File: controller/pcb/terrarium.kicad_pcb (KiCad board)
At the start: 2 copper layers, 90 x 90 mm, 55 parts, among them Q1 S8050, Q2 S8050, Q3 S8050, SW1 SW_Push, SW2 SW_Push, U1 ESP32-WROOM-32, U2 DS3231M, U3 LM1117-3.3

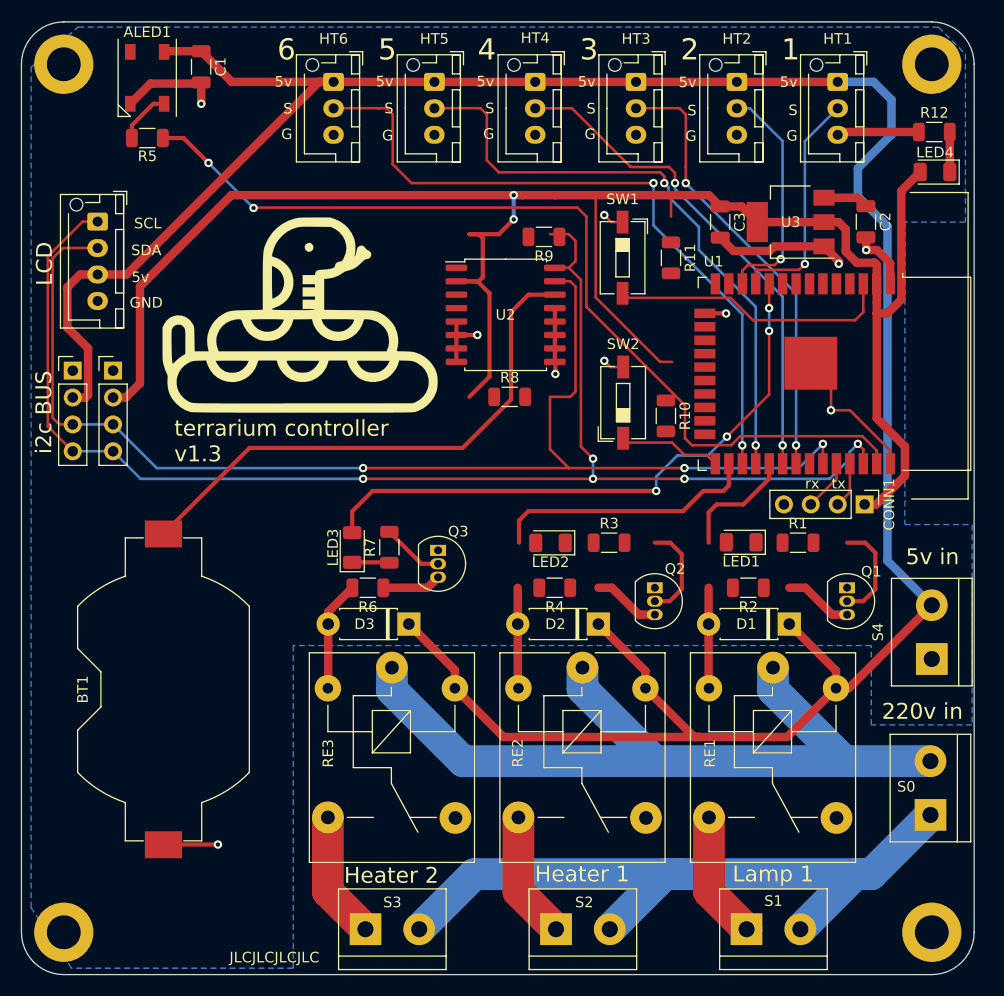
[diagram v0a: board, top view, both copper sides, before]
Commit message: pcb: developing smd layout
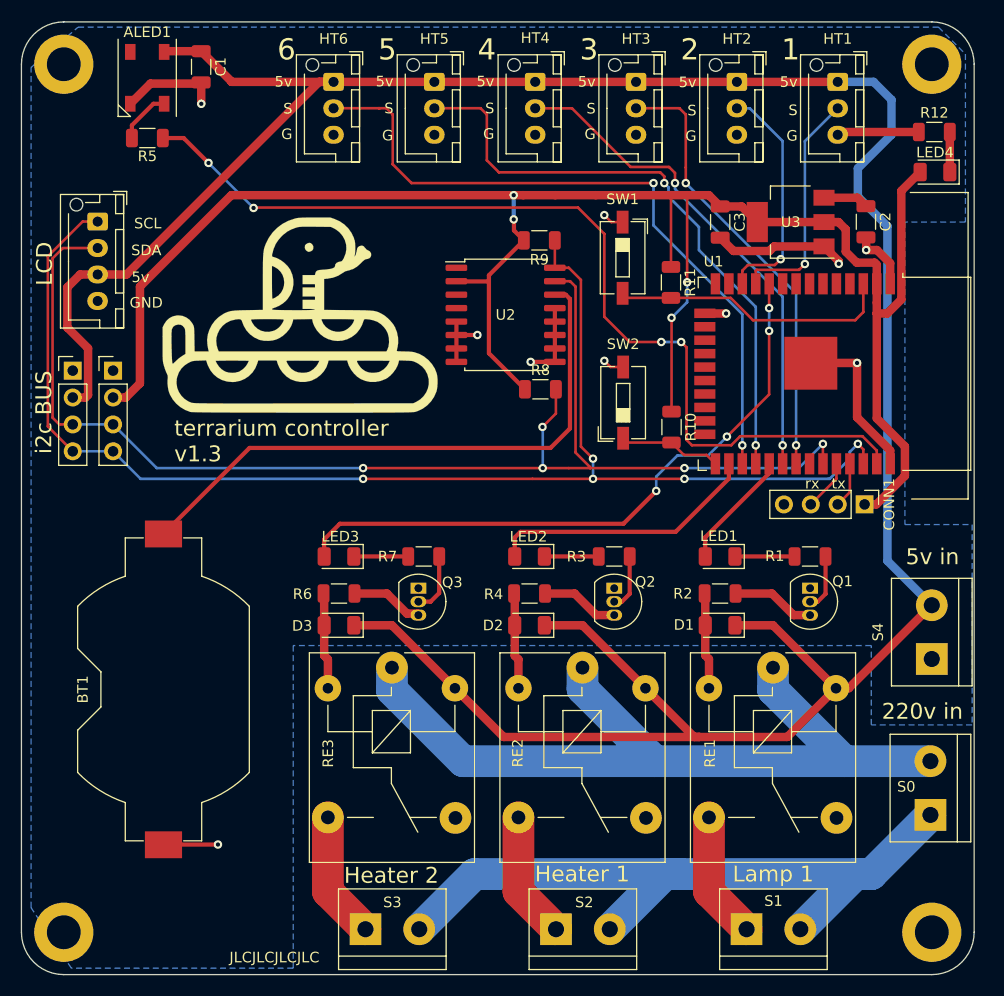
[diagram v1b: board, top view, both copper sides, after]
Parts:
- D1, D2, D3: footprint Diode_THT:D_DO-41_SOD81_P7.62mm_Horizontal -> Diode_SMD:D_1206_3216Metric
- moved D3 6.60 mm to (71.0, 80.0)
- moved D1 6.54 mm to (107.0, 80.0)
- moved D2 6.51 mm to (89.0, 80.0)
- moved Q3 4.03 mm to (78.5, 76.5)
- moved Q2 3.84 mm to (97.0, 76.5)
- moved Q1 3.50 mm to (115.5, 76.5)
- moved R7 3.36 mm to (79.0, 73.5), turned to 0 degrees
- moved R8 2.99 mm to (90.0, 57.7)
- moved R6 2.78 mm to (71.0, 77.0)
- moved R2 2.72 mm to (107.0, 77.0)
- moved R4 2.44 mm to (89.0, 77.0)
- moved LED1 2.40 mm to (107.0, 73.5)
- moved LED2 2.36 mm to (89.0, 73.5)
- moved R11 2.32 mm to (102.4, 47.6)
- moved R1 1.73 mm to (115.5, 73.5)
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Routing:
- net +5V: track 255.6 -> 268.0 mm
- net SDA: track 119.4 -> 125.1 mm, vias 3 -> 5
- net Net-(LED1-Pad1): track 0.00 -> 5.64 mm
- net GND: track 72.9 -> 78.3 mm
- net Net-(BT1-Pad1): track 51.2 -> 56.4 mm
- net Net-(LED2-Pad1): track 0.00 -> 5.14 mm
- net Net-(Q1-Pad2): track 9.63 -> 5.30 mm
- net Net-(Q2-Pad2): track 9.30 -> 5.30 mm
- net G25: track 57.2 -> 60.6 mm
- net SCL: track 132.2 -> 129.3 mm
- net G23: track 88.4 -> 91.3 mm, vias 2 -> 4
- net +3V3: track 181.9 -> 183.9 mm, vias 2 -> 4
- net Net-(LED3-Pad1): track 3.53 -> 5.14 mm
- net Net-(Q1-Pad3): track 6.51 -> 7.88 mm
- net Net-(Q3-Pad3): track 5.58 -> 6.93 mm
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
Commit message: Add copper plate, minor changes
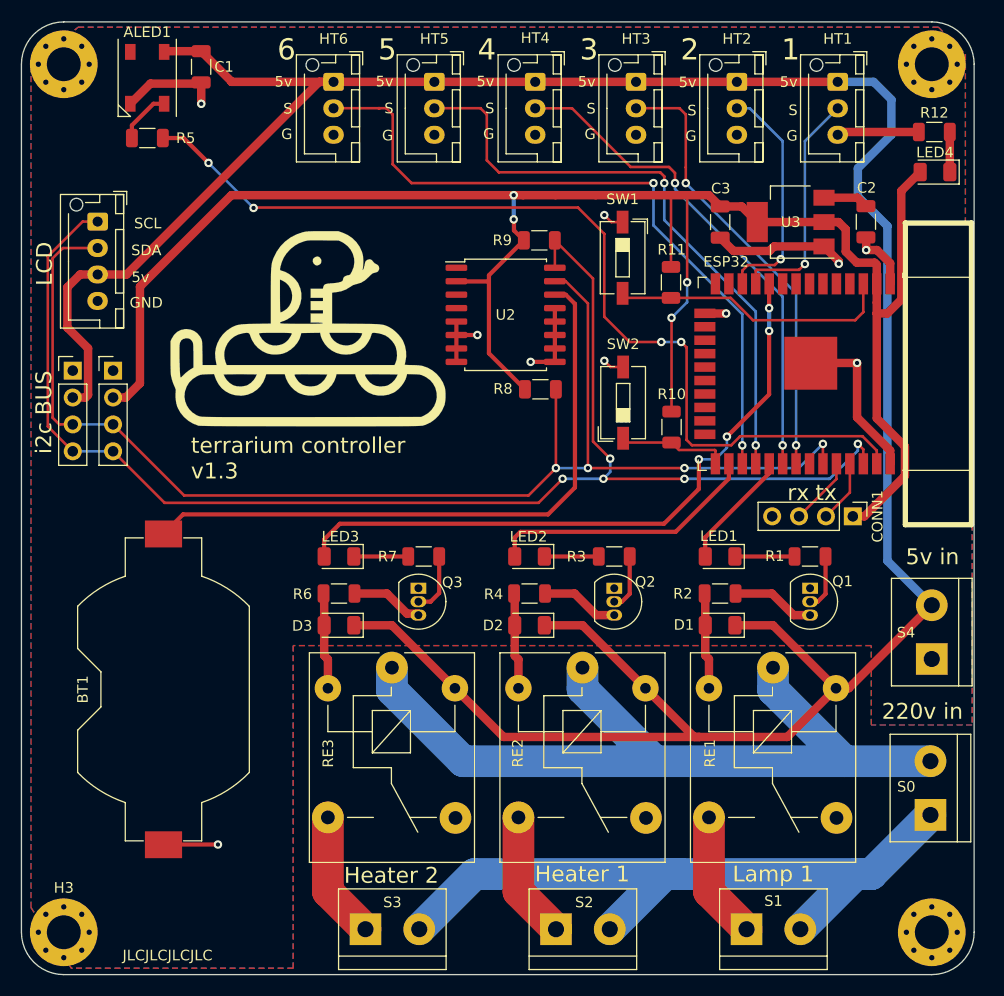
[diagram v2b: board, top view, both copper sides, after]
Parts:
- H1, H2, H3, H4: footprint MountingHole:MountingHole_3.2mm_M3_DIN965_Pad -> MountingHole:MountingHole_3.2mm_M3_Pad_Via
- moved CONN1 1.58 mm to (119.5, 69.7)
- moved G*** 1.49 mm to (68.1, 52.0)
- renumbered U1 to ESP32
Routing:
- net SCL: track 129.3 -> 134.0 mm
- net Net-(BT1-Pad1): track 56.4 -> 60.3 mm
- net RX: track 4.84 -> 6.42 mm
- net TX: track 4.31 -> 5.90 mm
- net +3V3: track 183.9 -> 185.5 mm
- net G25: track 60.6 -> 62.0 mm
- net SDA: track 125.1 -> 126.4 mm, vias 5 -> 4
- net Net-(R10-Pad2): track 9.72 -> 10.5 mm
- added copper zone on F.Cu, net +5V

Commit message: pcb: v1.3 minor changes
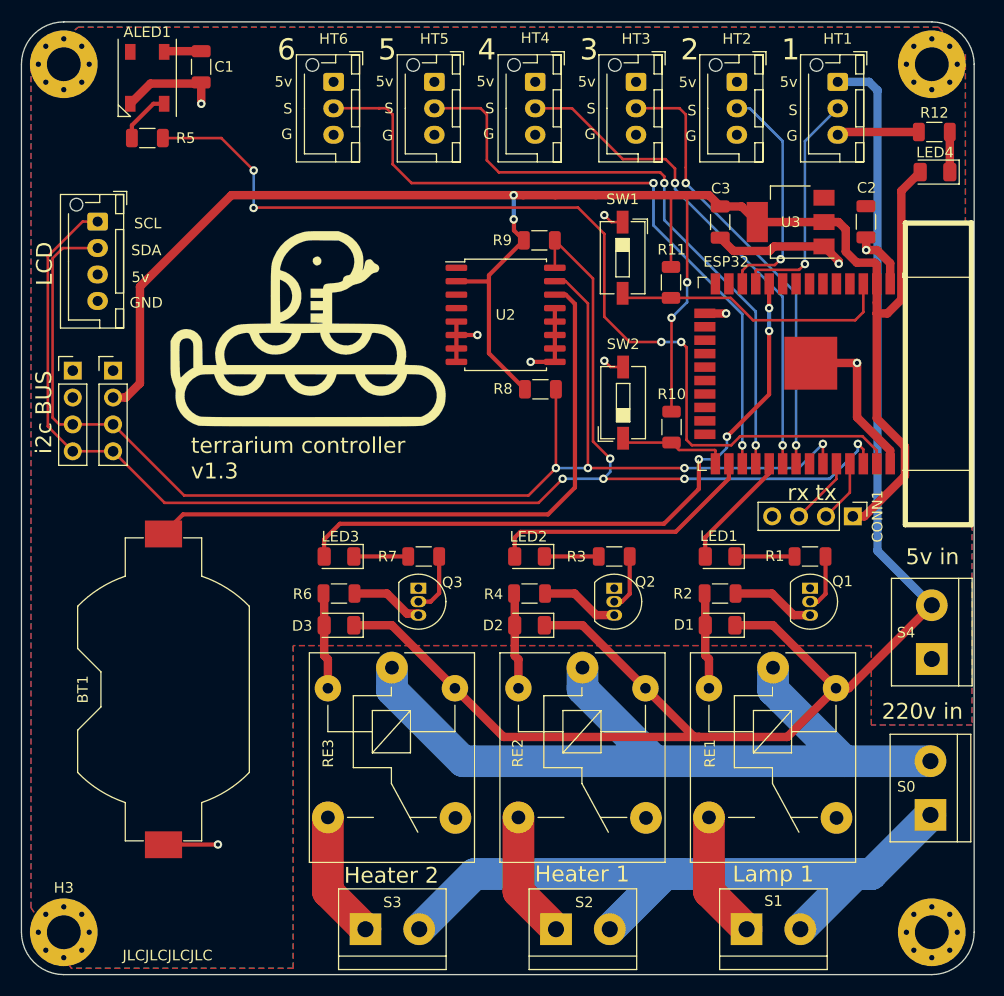
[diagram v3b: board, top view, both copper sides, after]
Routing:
- net +5V: track 268.0 -> 153.7 mm
- net G23: track 91.3 -> 93.3 mm

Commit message: pcb updates
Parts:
- SW1: value SW_Push -> RESET
- SW2: value SW_Push -> BOOT
- moved BT1 3.99 mm to (54.2, 90.0)
- moved i2c3 1.63 mm to (46.2, 57.5)
- moved i2c4 1.63 mm to (50.0, 57.5)
- renumbered ESP32 to U1, CONN1 to UART
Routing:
- net Net-(BT1-Pad1): track 60.3 -> 65.1 mm
- net SCL: track 134.0 -> 137.3 mm
- net SDA: track 126.4 -> 129.5 mm
- net +3V3: track 185.5 -> 186.9 mm
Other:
- board text added: "3v3"
- board text added: "Rx"
- board text added: "Tx"
- board text removed: "rx"
- board text removed: "tx"

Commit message: pcb: updates
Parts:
- added D4: 1N47xxA, Diode_SMD:D_1206_3216Metric, F.Cu at (54.1, 70.2)
- added SW3: RESET RTC, Button_Switch_SMD:SW_DIP_SPSTx01_Slide_6.7x4.1mm_W6.73mm_P2.54mm_LowProfile_JPin, F.Cu at (46.2, 72.8)
- renumbered UART to UART1
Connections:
- U2 pad 14: Net-(BT1-Pad1) -> Net-(D4-Pad1)
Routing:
- net Net-(D4-Pad1): track 0.00 -> 59.5 mm
- net Net-(BT1-Pad1): track 65.1 -> 8.35 mm
- net Net-(D4-Pad2): track 0.00 -> 6.79 mm
- net GND: track 78.3 -> 79.4 mm
- net G27: track 23.6 -> 24.6 mm
- net G26: track 23.1 -> 24.0 mm
- net Net-(R11-Pad2): track 26.8 -> 27.5 mm

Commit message: pcb v1.3 finished
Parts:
- D1, D2, D3: value 1N47xxA -> M7; footprint Diode_SMD:D_1206_3216Metric -> Diode_SMD:D_2114_3652Metric
- moved D1 0.81 mm to (107.8, 79.9)
- moved D2 0.77 mm to (89.8, 79.9)
- moved D3 0.74 mm to (71.7, 79.9)
- moved LED1 0.64 mm to (107.0, 72.9)
- moved LED2 0.64 mm to (89.0, 72.9)
- moved LED3 0.64 mm to (71.0, 72.9)
- moved Q1 0.64 mm to (115.5, 75.9)
- moved Q2 0.64 mm to (97.0, 75.9)
- moved Q3 0.64 mm to (78.5, 75.9)
- moved R1 0.64 mm to (115.5, 72.9)
- moved R2 0.64 mm to (107.0, 76.4)
- moved R3 0.64 mm to (97.0, 72.9)
- moved R4 0.64 mm to (89.0, 76.4)
- moved R6 0.64 mm to (71.0, 76.4)
- moved R7 0.64 mm to (79.0, 72.9)
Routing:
- net +5V: track 153.7 -> 152.5 mm
- net Net-(D1-Pad2): track 9.17 -> 9.89 mm
- net Net-(D3-Pad2): track 9.25 -> 9.97 mm
- net Net-(D2-Pad2): track 9.21 -> 9.94 mm
- net G5: track 11.3 -> 10.6 mm
- net G4: track 25.7 -> 25.2 mm

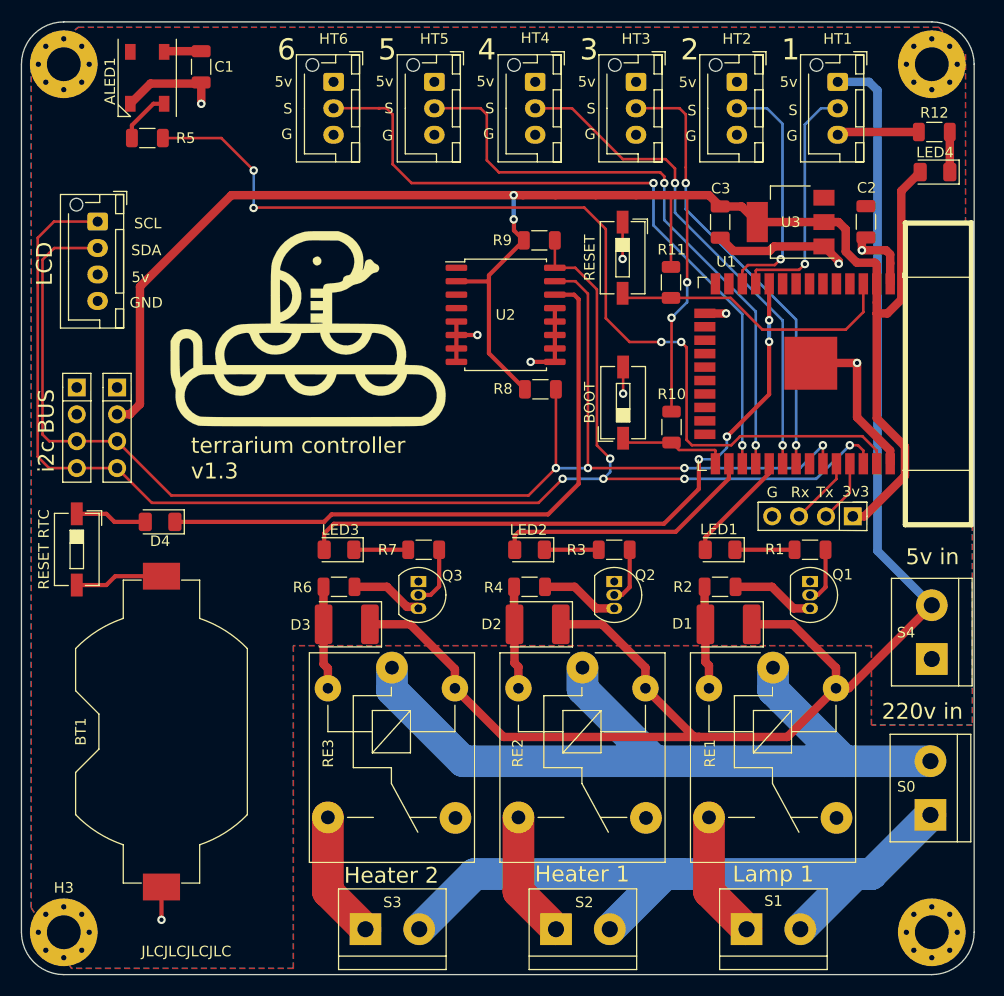
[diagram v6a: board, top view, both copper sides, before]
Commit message: Pcb/v1.4 (#3)
* pcb: refactor

* minor updates, bjt to sot-23

* rtc charge, refactoring

* update jst footprints, added missing 3d models

* refactoring

* minor changes

* diode for battery

* fix bugs in UART

* add transistor for sensors

* move status led from relay circuit

* pcb v1.4 release

* fix snake logo

Co-authored-by: Grigorii Merkushev <brushknight@pop-os.localdomain>
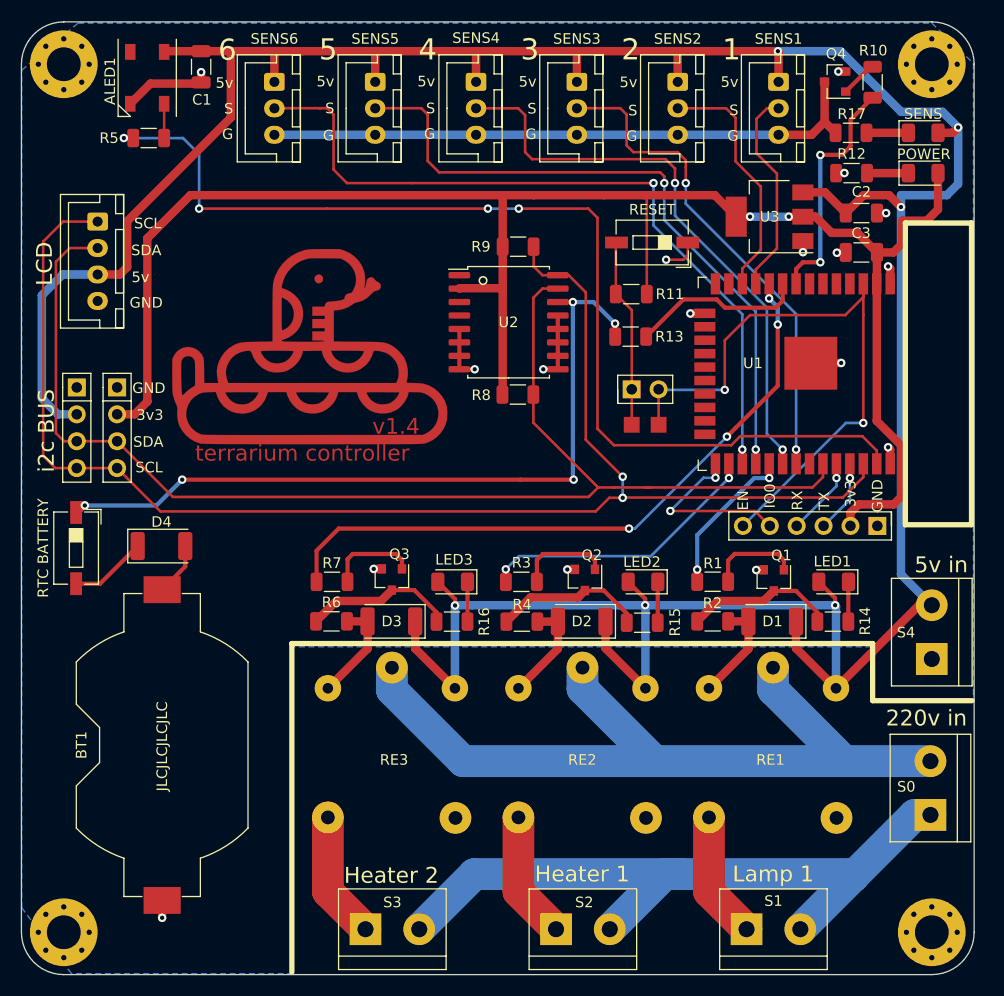
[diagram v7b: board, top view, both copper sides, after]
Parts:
- removed HT2, HT6: 4, Connector_JST:JST_XH_B3B-XH-AM_1x03_P2.50mm_Vertical
- removed HT3: 1, Connector_JST:JST_XH_B3B-XH-AM_1x03_P2.50mm_Vertical
- removed HT4: 2, Connector_JST:JST_XH_B3B-XH-AM_1x03_P2.50mm_Vertical
- removed HT5: 3, Connector_JST:JST_XH_B3B-XH-AM_1x03_P2.50mm_Vertical
- removed SW2: BOOT, Button_Switch_SMD:SW_DIP_SPSTx01_Slide_6.7x4.1mm_W6.73mm_P2.54mm_LowProfile_JPin
- removed UART1: data, Connector_PinHeader_2.54mm:PinHeader_1x04_P2.54mm_Vertical
- added LED5: SENS, LED_SMD:LED_1206_3216Metric, F.Cu at (126.2, 33.5)
- added Q4: S8050, Package_TO_SOT_SMD:SOT-23, F.Cu at (117.9, 28.6)
- added R13: 100k, Resistor_SMD:R_1206_3216Metric, F.Cu at (98.6, 52.7)
- added R14: 5k, Resistor_SMD:R_1206_3216Metric, F.Cu at (117.7, 79.7)
- added R15: 5k, Resistor_SMD:R_1206_3216Metric, F.Cu at (99.6, 79.8)
- added R16: 5k, Resistor_SMD:R_1206_3216Metric, F.Cu at (81.7, 79.7)
- added R17: 5k, Resistor_SMD:R_1206_3216Metric, F.Cu at (119.4, 33.5)
- added RESET_j1: data, Connector_PinHeader_2.54mm:PinHeader_1x02_P2.54mm_Vertical, F.Cu at (98.7, 57.7)
- added SENS2: 4, Connector_JST:JST_XH_B3B-XH-AM_1x03_P2.50mm_Vertical, F.Cu at (103.0, 28.7)
- added SENS3: 1, Connector_JST:JST_XH_B3B-XH-AM_1x03_P2.50mm_Vertical, F.Cu at (93.5, 28.7)
- added SENS4: 2, Connector_JST:JST_XH_B3B-XH-AM_1x03_P2.50mm_Vertical, F.Cu at (83.9, 28.7)
- added SENS5: 3, Connector_JST:JST_XH_B3B-XH-AM_1x03_P2.50mm_Vertical, F.Cu at (74.4, 28.7)
- added SENS6: 4, Connector_JST:JST_XH_B3B-XH-AM_1x03_P2.50mm_Vertical, F.Cu at (64.9, 28.7)
- added TP1: TestPoint, TestPoint:TestPoint_Pad_1.5x1.5mm, F.Cu at (101.2, 61.1)
- added TP2: TestPoint, TestPoint:TestPoint_Pad_1.5x1.5mm, F.Cu at (98.7, 61.1)
- added UART: data, Connector_PinHeader_2.54mm:PinHeader_1x06_P2.54mm_Vertical, F.Cu at (121.9, 70.6)
- D1, D2, D3: footprint Diode_SMD:D_2114_3652Metric -> Diode_SMD:D_2010_5025Metric
- D4: footprint Diode_SMD:D_1206_3216Metric -> Diode_SMD:D_2010_5025Metric
- Q1, Q2, Q3: footprint Package_TO_SOT_THT:TO-92_Inline -> Package_TO_SOT_SMD:SOT-23
- R10: value 10k -> 150ohm
- R12: value 300 -> 5k
- R2, R4, R6: value R_Small -> 10
- SW3: value RESET RTC -> RTC BATTERY
- moved R10 37.7 mm to (121.4, 28.7), turned to 90 degrees
- moved C3 13.6 mm to (120.3, 44.8), turned to 180 degrees
- moved LED3 11.2 mm to (81.7, 75.9)
- moved LED1 11.1 mm to (117.7, 75.9)
- moved LED2 11.1 mm to (99.7, 75.9)
- moved R1 9.69 mm to (106.3, 75.9)
- moved R3 9.28 mm to (88.2, 75.9)
- moved R7 9.17 mm to (70.3, 75.9)
- moved R12 8.73 mm to (119.4, 37.3)
- moved SENS1 5.59 mm to (112.5, 28.7)
- moved D3 4.22 mm to (75.9, 79.6)
- moved D2 4.17 mm to (93.9, 79.6)
- moved D1 4.13 mm to (111.9, 79.6)
- moved R11 3.91 mm to (98.6, 48.7), turned to 180 degrees
- moved Q1 3.42 mm to (112.1, 75.8)
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- renumbered HT1 to SENS1
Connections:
- D4 pad 2: Net-(D4-Pad2) -> Net-(BT1-Pad1)
- LED1 pad 2: G5 -> +5V
- LED2 pad 2: G4 -> +5V
- LED3 pad 2: G25 -> +5V
- Q1 pad 1: GND -> Net-(Q1-Pad1)
- Q1 pad 2: Net-(Q1-Pad2) -> GND
- Q2 pad 1: GND -> Net-(Q2-Pad1)
- Q2 pad 2: Net-(Q2-Pad2) -> GND
- Q3 pad 1: GND -> Net-(Q3-Pad1)
- Q3 pad 2: Net-(Q3-Pad2) -> GND
- R1 pad 1: Net-(LED1-Pad1) -> G5
- R1 pad 2: Net-(Q1-Pad2) -> Net-(Q1-Pad1)
- R10 pad 1: +3V3 -> G32
- R10 pad 2: Net-(R10-Pad2) -> Net-(Q4-Pad1)
- R3 pad 1: Net-(LED2-Pad1) -> G4
- R3 pad 2: Net-(Q2-Pad2) -> Net-(Q2-Pad1)
- R7 pad 1: Net-(LED3-Pad1) -> G25
- R7 pad 2: Net-(Q3-Pad2) -> Net-(Q3-Pad1)
- SENS1 pad 3: GND -> Net-(Q4-Pad3)
- SW3 pad 1: Net-(D4-Pad2) -> Net-(R13-Pad2)
- SW3 pad 2: Net-(BT1-Pad1) -> Net-(D4-Pad1)
- U1 pad 25: Net-(R10-Pad2) -> IO0
- U1 pad 3: Net-(R11-Pad2) -> EN
- U1 pad 8: Net-(U1-Pad8) -> G32
- U1 pad 9: Net-(U1-Pad9) -> G33
- U2 pad 14: Net-(D4-Pad1) -> Net-(R13-Pad2)
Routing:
- net +5V: track 152.5 -> 312.0 mm, vias 0 -> 6
- net Net-(R13-Pad2): track 0.00 -> 72.6 mm, vias 0 -> 5
- net EN: track 0.00 -> 58.9 mm, vias 0 -> 2
- net Net-(Q4-Pad3): track 0.00 -> 58.1 mm
- net Net-(D4-Pad1): track 59.5 -> 7.29 mm
- net GND: track 79.4 -> 42.2 mm, vias 10 -> 17
- net G32: track 0.00 -> 22.8 mm, vias 0 -> 2
- net +3V3: track 186.9 -> 167.4 mm, vias 4 -> 2
- net IO0: track 0.00 -> 16.9 mm, vias 0 -> 2
- net G33: track 0.00 -> 16.6 mm
- net Net-(R10-Pad2): track 10.5 -> 0.00 mm
- net Net-(R11-Pad2): track 27.5 -> 17.9 mm
- net Net-(Q2-Pad1): track 0.00 -> 8.92 mm
- net Net-(Q1-Pad1): track 0.00 -> 8.69 mm
- net Net-(Q3-Pad1): track 0.00 -> 8.65 mm
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- removed copper zone on F.Cu, net +5V
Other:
- board text added: "EN"
- board text added: "IO0"
- board text added: "RX"
- board text added: "TX"
- board text added: "terrarium controller"
- board text added: "terrarium controller v1.4 github.com/brushknight/terrarium github.com/brushknight/terrarium-hardware"
- board text added: "v1.4"
- board text removed: "Rx"
- board text removed: "Tx"
- board text removed: "terrarium controller v1.3"
- board text removed: "terrarium controller v1.3 github.com/brushknight/terrarium github.com/brushknight/terrarium-hardware"
